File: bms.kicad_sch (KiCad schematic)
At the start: 50 parts, among them J9 BAT_PORT, Q16 TPN2R203NC, Q5 AON7544, Q6 AON7544, U7 MAX17320G22+

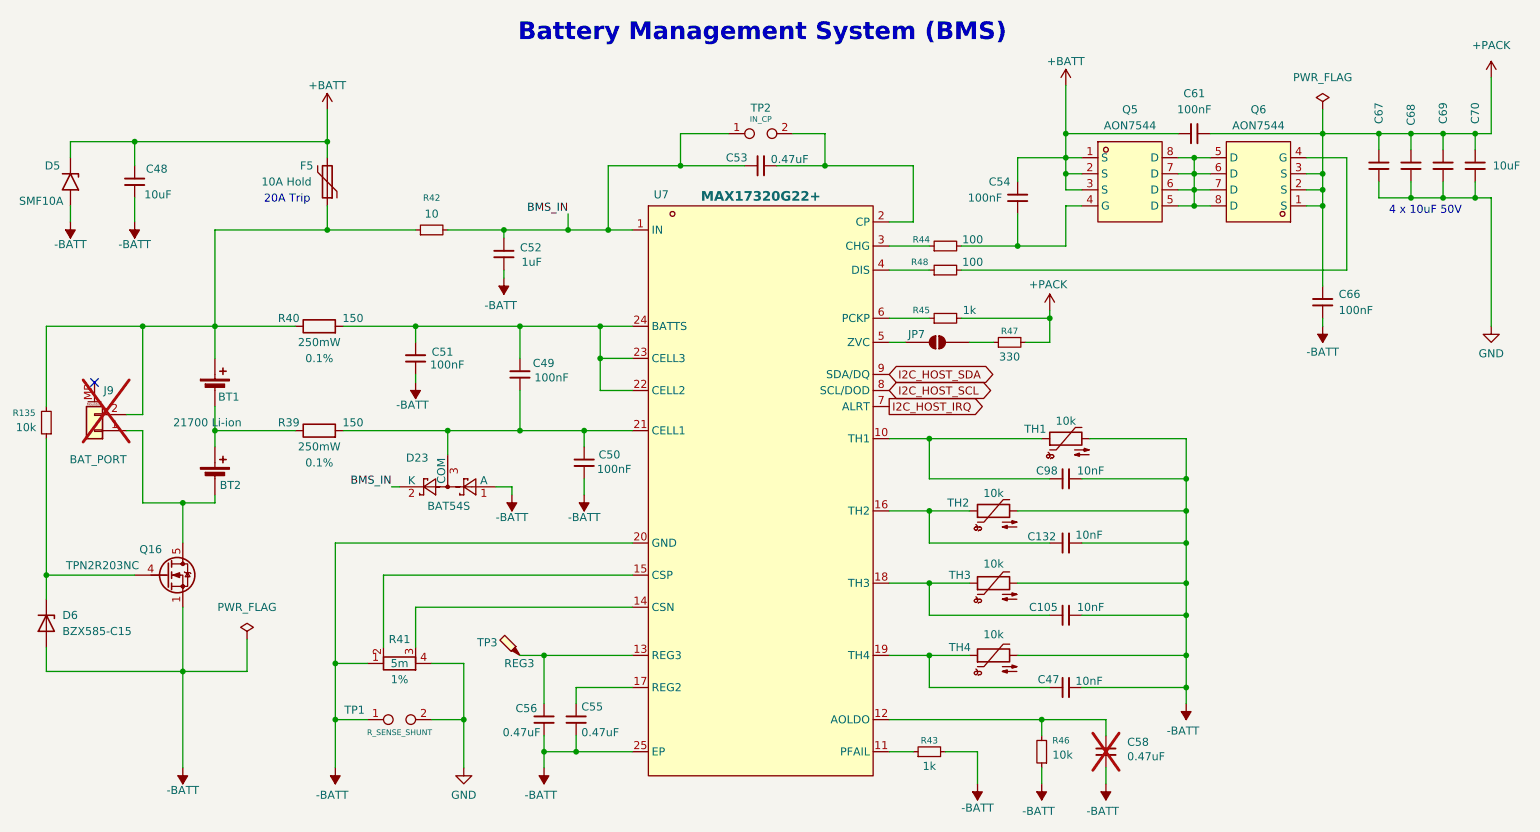
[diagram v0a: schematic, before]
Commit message: checkpoint: schematic WIP before battery -> charger rename
Connectors and Overview sheets, LSM6DSV16X/TPS22945/charger datasheets,
and in-progress edits across all sheets, committed as-is so the rename
diff stands alone.

Co-Authored-By: Claude Opus 5.5 <noreply@anthropic.com>
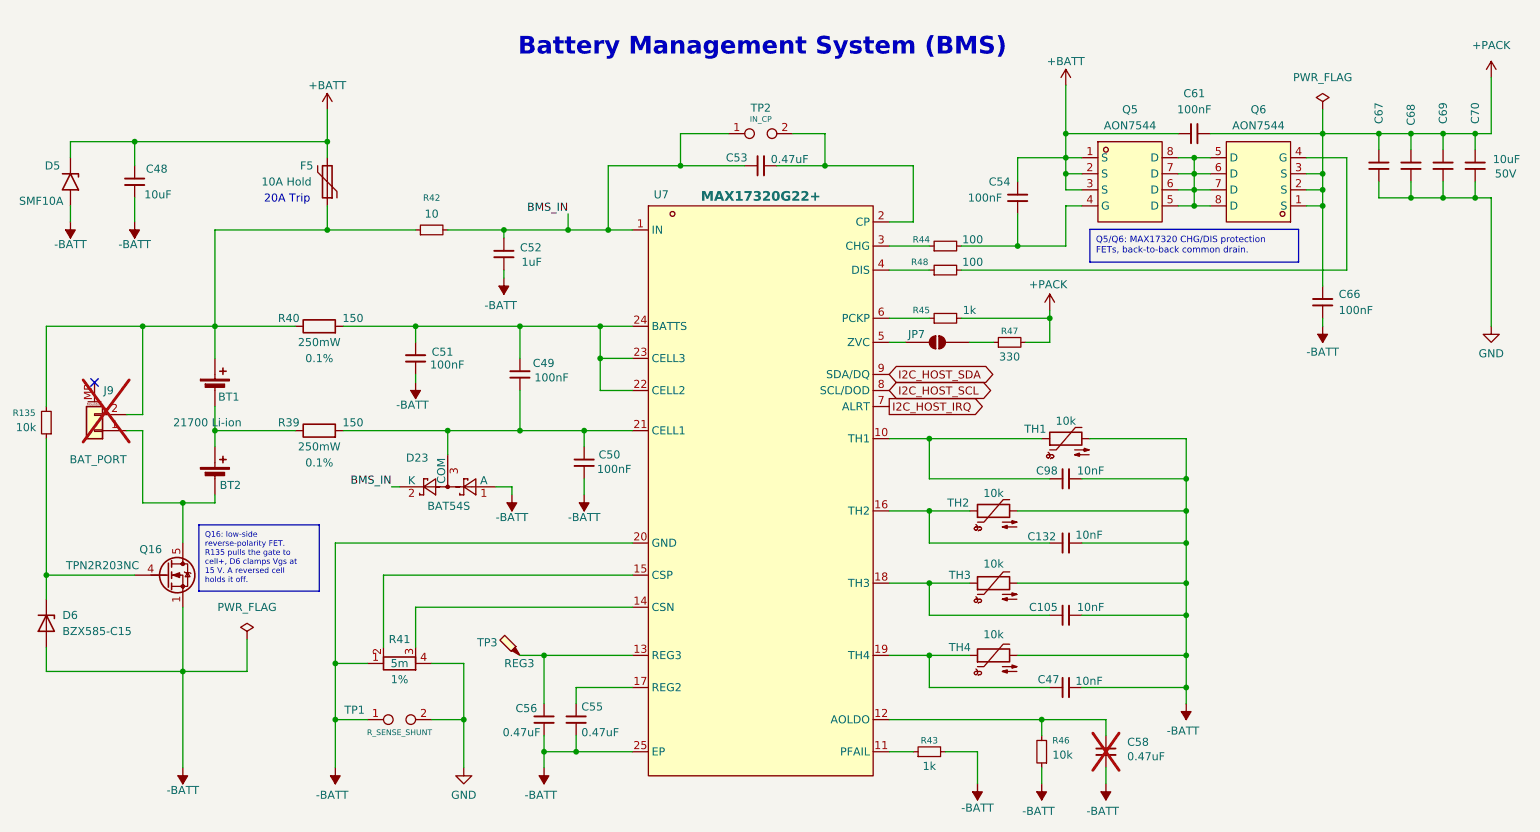
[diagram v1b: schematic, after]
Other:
- note added: "${TITLE}"
- note removed: "4 x 10uF 50V"
- note removed: "Battery Management System (BMS)"
- title: Battery Managment System (BMS) -> Battery Management System (BMS)
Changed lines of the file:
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@@
 	(paper "A4")
 	(title_block
-		(title "Battery Managment System (BMS)")
+		(title "Battery Management System (BMS)")
 		(date "2026-09-27")
 		(company "LimesKey")
 	)
-	(text "Battery Management System (BMS)"
+	(text "${TITLE}"
 		(exclude_from_sim no)
-		(at 156.464 36.068 0)
+		(at 156.464 38.354 0)
 		(effects
 			(font
@@
 		)
 	)
-	(text "4 x 10uF 50V"
+	(text "20A Trip"
 		(exclude_from_sim no)
-		(at 261.366 64.262 0)
+		(at 81.28 62.484 0)
 		(effects
 			(font
@@
 		)
 	)
-	(text "20A Trip"
+	(text_box "Q16: low-side reverse-polarity FET. R135 pulls the gate to cell+, D6 clamps Vgs at 15 V. A reversed cell holds it off."
 		(exclude_from_sim no)
-		(at 81.28 62.484 0)
+		(at 67.31 113.9688 0)
+		(size 19.05 10.4912)
+		(margins 0.9525 0.9525 0.9525 0.9525)
+		(stroke
+			(width 0)
+			(type solid)
+		)
+		(fill
+			(type none)
+		)
 		(effects
 			(font
-				(size 1.27 1.27)
+				(size 0.889 0.889)
 			)
+			(justify left top)
+		)
+	)
+	(text_box "Q5/Q6: MAX17320 CHG/DIS protection FETs, back-to-back common drain."
+		(exclude_from_sim no)
+		(at 208.28 67.2148 0)
+		(size 33.02 5.1752)
+		(margins 0.9525 0.9525 0.9525 0.9525)
+		(stroke
+			(width 0)
+			(type solid)
+		)
+		(fill
+			(type none)
+		)
+		(effects
+			(font
+				(size 1.016 1.016)
+			)
+			(justify left top)
 		)
 	)
@@
 		)
 		(property "Value" "10uF"
-			(at 272.034 57.15 0)
+			(at 272.034 56.134 0)
 			(show_name no)
 			(do_not_autoplace no)
@@
 		)
 		(property "Voltage Rating" "50V"
-			(at 269.24 57.15 0)
-			(hide yes)
+			(at 274.066 58.42 0)
 			(show_name no)
 			(do_not_autoplace no)
